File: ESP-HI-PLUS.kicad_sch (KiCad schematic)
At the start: 87 parts, among them J1 USB_C_Receptacle_USB2.0_14P, J2 2" IPS LCD, J3 PR5L4015-5P-C-F, J4 PR5L4015-5P-C-F, J5 Micro_SD_Card, Q1 AO3401A, Q2 NTK3139P, SW1 SKRPACE010, SW2 SKRPACE010, SW3 JS102011SAQN, U1 MAX40200AUK, U2 ESP32-S3-WROOM-1, U3 TLV75733PDBV, U5 TP4065, U6 MAX40200AUK, U7 MAX98357A, U8 LSM6DSV16X

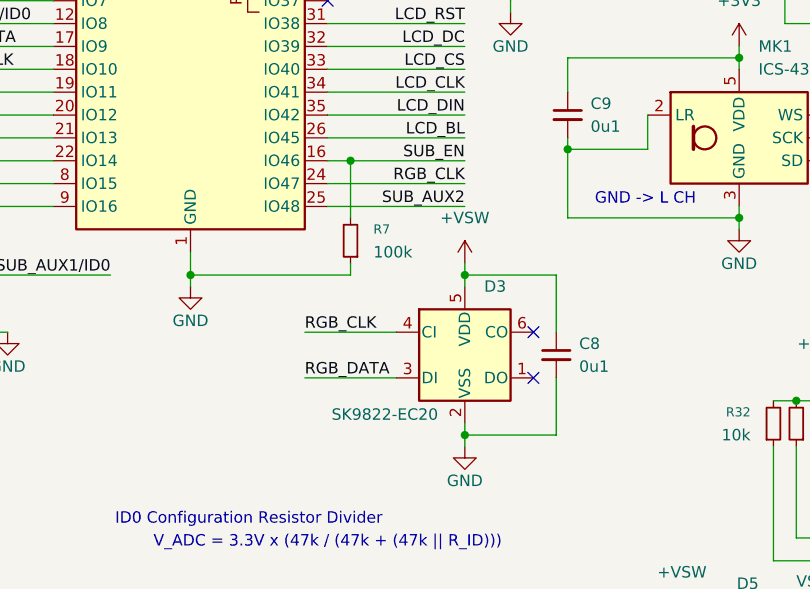
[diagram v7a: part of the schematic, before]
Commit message: ESP-HI-PLUS v1.17: Changed RGB LED to 2020 NeoPixel
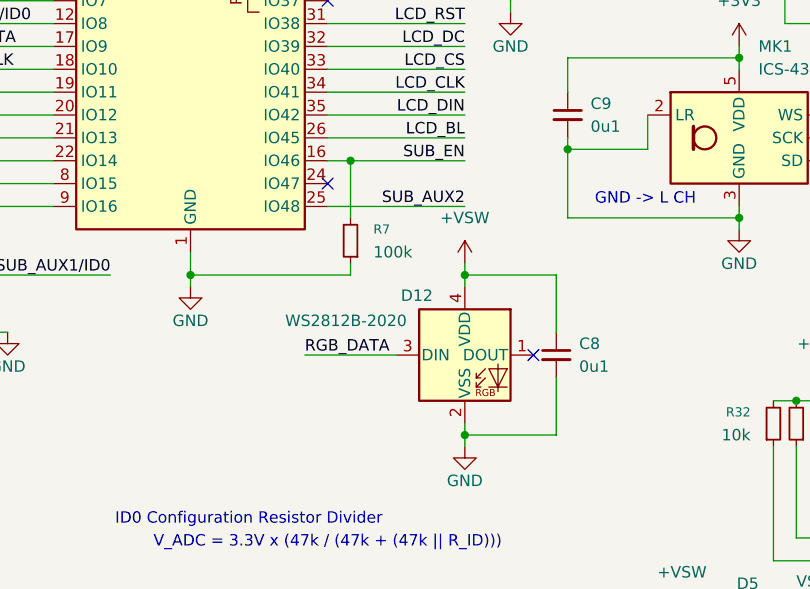
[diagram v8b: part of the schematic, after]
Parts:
- removed D3: SK9822-EC20, PCM_SparkFun-LED:APA102_2020-6Pin, symbol PCM_SparkFun-LED:APA102_2020-6Pin
- added D12: WS2812B-2020, LED_SMD:LED_WS2812B-2020_PLCC4_2.0x2.0mm, symbol LED:WS2812B-2020
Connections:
- net +VSW: now also D12.4 (VDD)
- net GND: now also D12.2 (VSS)
- net RGB_DATA: now also D12.3 (DIN)
- net RGB_CLK: no longer names the net of U2.24 (IO47)
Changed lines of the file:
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@@
 		(title "ESP-HI-PLUS")
 		(date "2026-07-20")
-		(rev "v1.0")
+		(rev "v1.17")
 	)
 	(text "V_ADC = 3.3V x (47k / (47k + (47k || R_ID)))"
@@
 	)
 	(no_connect
-		(at 107.95 91.44)
+		(at 85.09 69.85)
 	)
 	(no_connect
-		(at 107.95 86.36)
+		(at 107.95 88.9)
 	)
 	(no_connect
@@
 	(wire
 		(pts
-			(xy 82.55 86.36) (xy 92.71 86.36)
-		)
-		(stroke
-			(width 0)
-			(type default)
-		)
-	)
-	(wire
-		(pts
 			(xy 154.94 133.35) (xy 157.48 133.35)
 		)
@@
 	(wire
 		(pts
-			(xy 85.09 69.85) (xy 100.33 69.85)
-		)
-		(stroke
-			(width 0)
-			(type default)
-		)
-	)
-	(wire
-		(pts
 			(xy 241.3 77.47) (xy 256.54 77.47)
 		)
@@
 	(wire
 		(pts
-			(xy 82.55 91.44) (xy 92.71 91.44)
+			(xy 82.55 88.9) (xy 92.71 88.9)
 		)
 		(stroke
@@
 	)
 	(label "RGB_DATA"
-		(at 82.55 91.44 0)
+		(at 82.55 88.9 0)
 		(effects
 			(font
@@
 		)
 	)
-	(label "RGB_CLK"
-		(at 82.55 86.36 0)
-		(effects
-			(font
-				(size 1.27 1.27)
-			)
-			(justify left bottom)
-		)
-	)
 	(label "SUB_I2C_SDA"
 		(at 189.23 87.63 0)
@@
 		)
 	)
-	(label "RGB_CLK"
-		(at 100.33 69.85 180)
-		(effects
-			(font
-				(size 1.27 1.27)
-			)
-			(justify right bottom)
-		)
-	)
 	(label "SUB_UTXD_C"
 		(at 240.03 60.96 180)
@@
 	)
 	(symbol
+		(lib_id "LED:WS2812B-2020")
+		(at 100.33 88.9 0)
+		(unit 1)
+		(body_style 1)
+		(exclude_from_sim no)
+		(in_bom yes)
+		(on_board yes)
+		(in_pos_files yes)
+		(dnp no)
+		(property "Reference" "D12"
+			(at 94.996 82.296 0)
+			(show_name no)
+			(do_not_autoplace no)
+			(effects
+				(font
+					(size 1.27 1.27)
+				)
+			)
+		)
+		(property "Value" "WS2812B-2020"
+			(at 87.122 85.09 0)
+			(show_name no)
+			(do_not_autoplace no)
+			(effects
+				(font
+					(size 1.27 1.27)
+				)
+			)
+		)
+		(property "Footprint" "LED_SMD:LED_WS2812B-2020_PLCC4_2.0x2.0mm"
+			(at 101.6 96.52 0)
+			(hide yes)
+			(show_name no)
+			(do_not_autoplace no)
+			(effects
+				(font
+					(size 1.27 1.27)
+				)
+				(justify left top)
+			)
+		)
+		(property "Datasheet" "https://cdn-shop.adafruit.com/product-files/4684/4684_WS2812B-2020_V1.3_EN.pdf"
+			(at 102.87 98.425 0)
+			(hide yes)
+			(show_name no)
+			(do_not_autoplace no)
+			(effects
+				(font
+					(size 1.27 1.27)
+				)
+				(justify left top)
+			)
+		)
+		(property "Description" "RGB LED with integrated controller, 2.0 x 2.0 mm, 12 mA"
+			(at 100.33 88.9 0)
+			(hide yes)
+			(show_name no)
+			(do_not_autoplace no)
+			(effects
+				(font
+					(size 1.27 1.27)
+				)
+			)
+		)
+		(pin "3"
+		)
+		(pin "1"
+		)
+		(pin "2"
+		)
+		(pin "4"
+		)
+		(instances
+			(project "ESP-HI-PLUS"
+				(path "/38bc51f5-c7e2-4cb9-a161-d419c07b2cad"
+					(reference "D12")
+					(unit 1)
+				)
+			)
+		)
+	)
+	(symbol
 		(lib_id "power:+BATT")
 		(at 151.13 154.94 0)
@@
 					(unit 1)
 				)
-			)
-		)
-	)
-	(symbol
-		(lib_id "PCM_SparkFun-LED:APA102_2020-6Pin")
-		(at 100.33 88.9 0)
-		(unit 1)
-		(body_style 1)
-		(exclude_from_sim no)
-		(in_bom yes)
-		(on_board yes)
-		(in_pos_files yes)
-		(dnp no)
-		(property "Reference" "D3"
-			(at 102.4733 81.28 0)
-			(show_name no)
-			(do_not_autoplace no)
-			(effects
-				(font
-					(size 1.27 1.27)
-				)
-				(justify left)
-			)
-		)
-		(property "Value" "SK9822-EC20"
-			(at 91.44 95.504 0)
-			(show_name no)
-			(do_not_autoplace yes)
-			(effects
-				(font
-					(size 1.27 1.27)
-				)
-			)
-		)
-		(property "Footprint" "PCM_SparkFun-LED:APA102_2020-6Pin"
-			(at 100.33 97.79 0)
-			(hide yes)
-			(show_name no)
-			(do_not_autoplace no)
-			(effects
-				(font
-					(size 1.27 1.27)
-				)
-				(justify top)
-			)
-		)
-		(property "Datasheet" "https://item.szlcsc.com/datasheet/SK9822-EC20/3185287.html?spm=sc.gbn.xds.a___sc.gbn.hd.ss&lcsc_vid=ElBaVFMHFFZdX1VWEQQPBVFeTgUKBVRWEVUKVFFVFVIxVlNeQ1JeU1JXRFBWUjsOAxUeFF5JWBEPFBcWGBMaSQ4KFE8NCAlJ"
-			(at 100.33 100.33 0)
-			(hide yes)
-			(show_name no)
-			(do_not_autoplace no)
-			(effects
-				(font
-					(size 1.27 1.27)
-				)
-				(justify top)
-			)
-		)
-		(property "Description" "SK9822 SMD 2x2mm 2-Wire Addressable RGB LED (6 pin)"
-			(at 100.33 106.68 0)
-			(hide yes)
-			(show_name no)
-			(do_not_autoplace no)
-			(effects
-				(font
-					(size 1.27 1.27)
-				)
-			)
-		)
-		(property "PROD_ID" "DIO-14111"
-			(at 100.33 104.14 0)
-			(hide yes)
-			(show_name no)
-			(do_not_autoplace no)
-			(effects
-				(font
-					(size 1.27 1.27)
-				)
-			)
-		)
-		(pin "1"
-		)
-		(pin "6"
-		)
-		(pin "3"
-		)
-		(pin "5"
-		)
-		(pin "2"
-		)
-		(pin "4"
-		)
-		(instances
-			(project "ESP-HI-PLUS"
-				(path "/38bc51f5-c7e2-4cb9-a161-d419c07b2cad"
-					(reference "D3")
-					(unit 1)
-				)
